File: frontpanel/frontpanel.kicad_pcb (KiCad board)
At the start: 2 copper layers, 50.5 x 128.5 mm, 13 parts

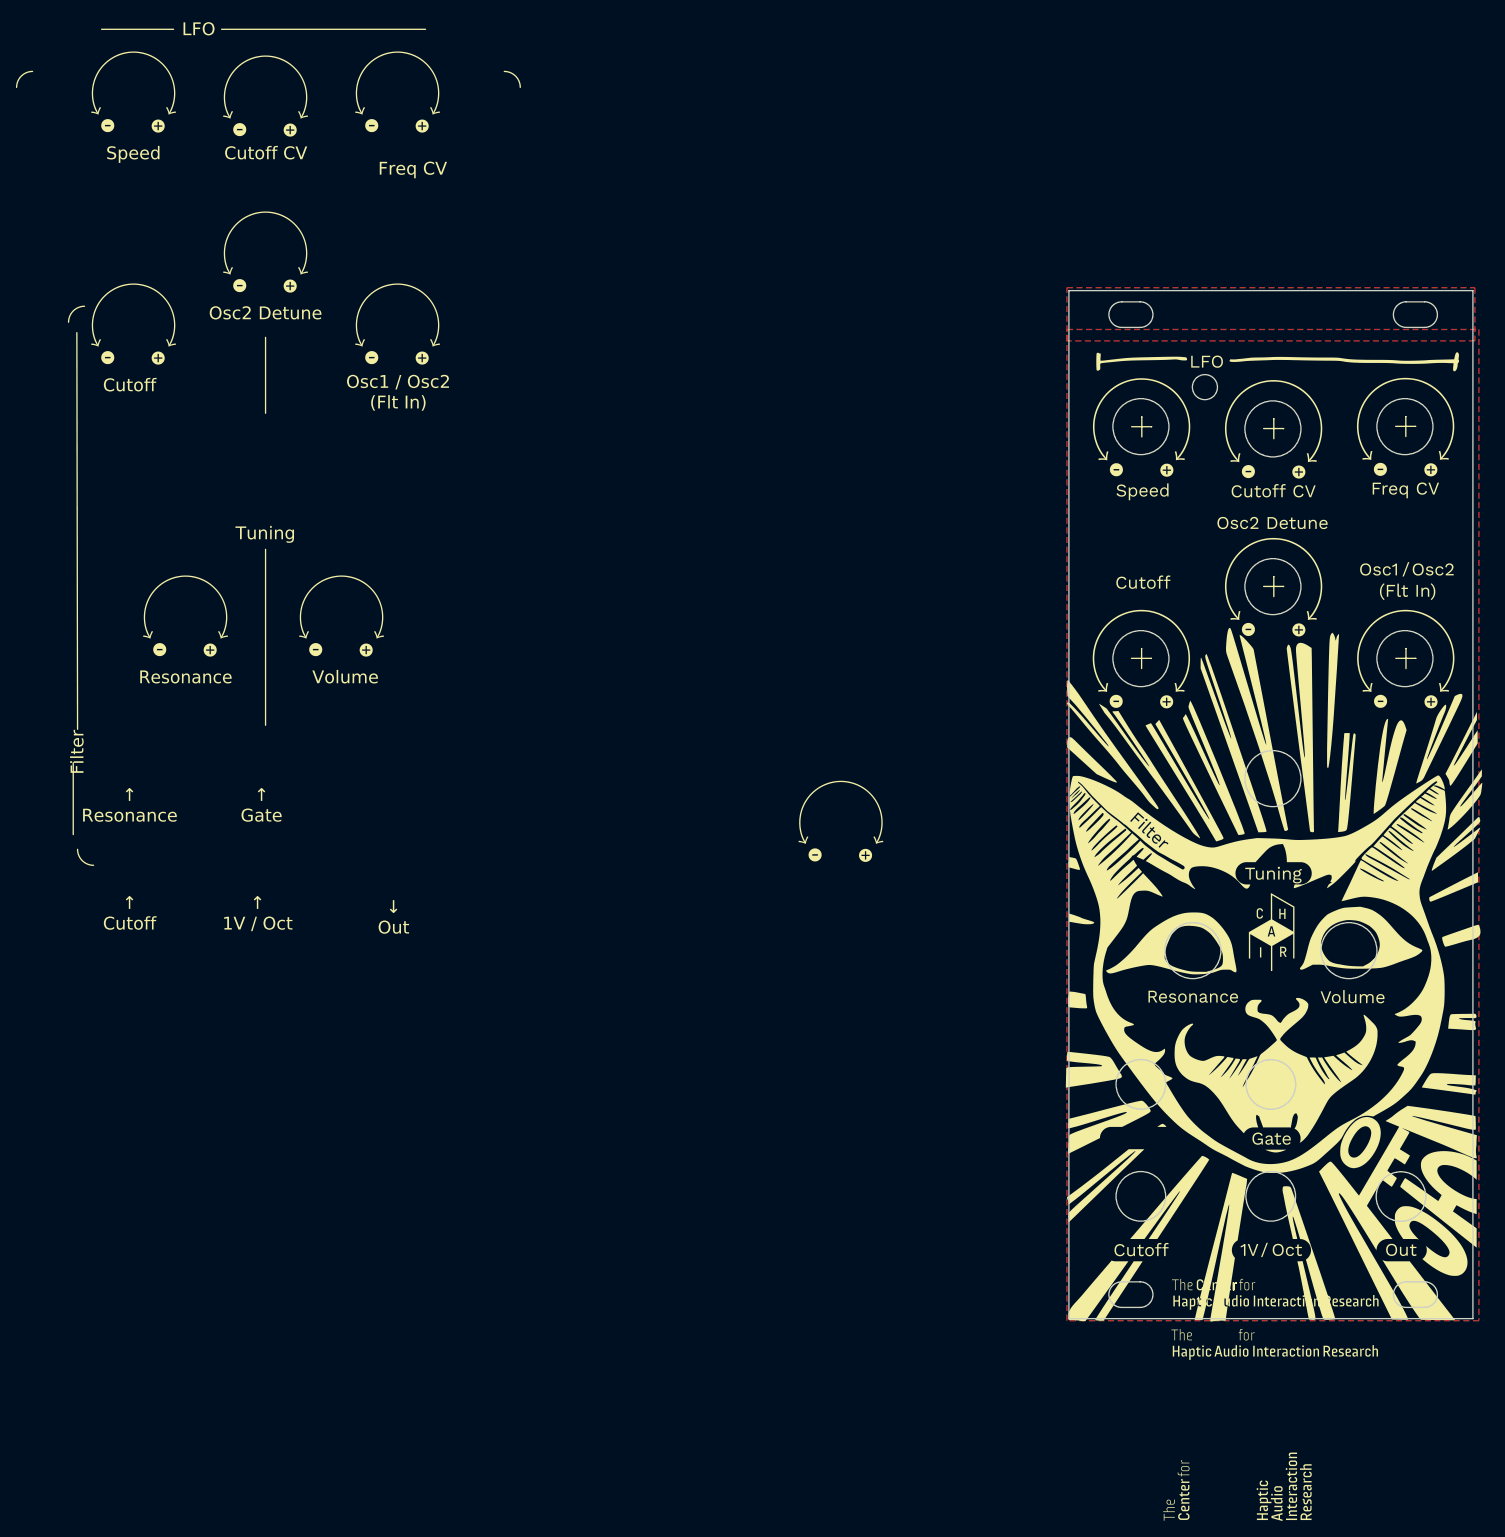
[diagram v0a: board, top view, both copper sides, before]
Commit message: Some fixes after evaluation of prototype
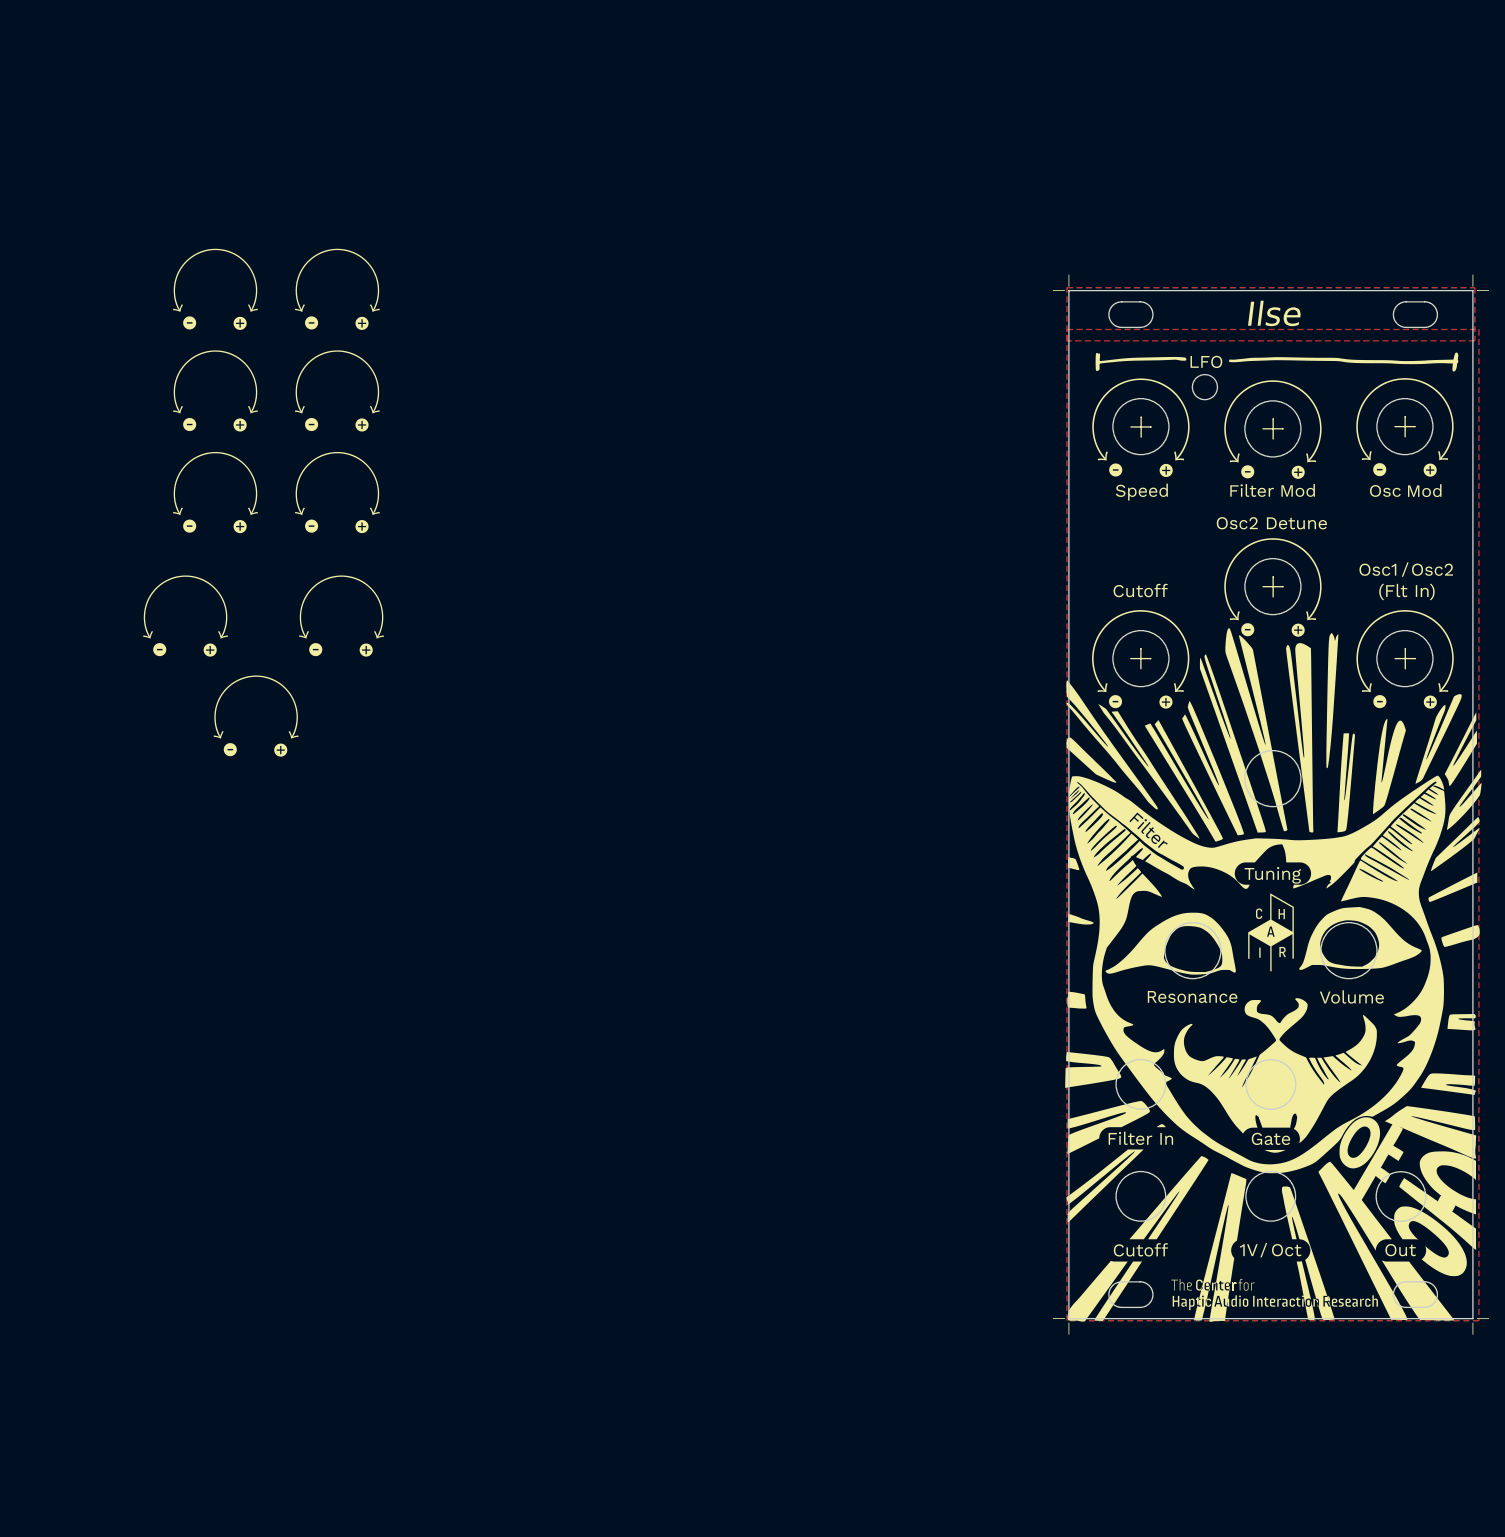
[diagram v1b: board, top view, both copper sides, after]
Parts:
- removed G***: LOGO, CHAIR:CHAIR_logo_horizontal_silkscreen+Cu
- moved REF** 74.3 mm to (-32.3, 90.2)
- moved REF** 51.1 mm to (-37.3, 62.2)
- moved REF** 33.1 mm to (-22.1, 62.2)
- moved REF** 25.8 mm to (-22.1, 36.8)
- moved REF** 25.0 mm to (-37.3, 36.8)
- moved REF** 18.5 mm to (-37.3, 49.5)
- moved REF** 11.2 mm to (-22.1, 49.5)
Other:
- board text removed: "Cutoff"
- board text removed: "Cutoff CV"
- board text removed: "Filter"
- board text removed: "Freq CV"
- board text removed: "LFO"
- board text removed: "Osc1 / Osc2 (Flt In)"
- board text removed: "Osc2 Detune"
- board text removed: "Resonance"
- board text removed: "Speed"
- board text removed: "Tuning"
- board text removed: "Volume"
- board text removed: "↑ 1V / Oct"
- board text removed: "↑ Cutoff"
- board text removed: "↑ Gate"
- board text removed: "↑ Resonance"
- board text removed: "↓ Out"

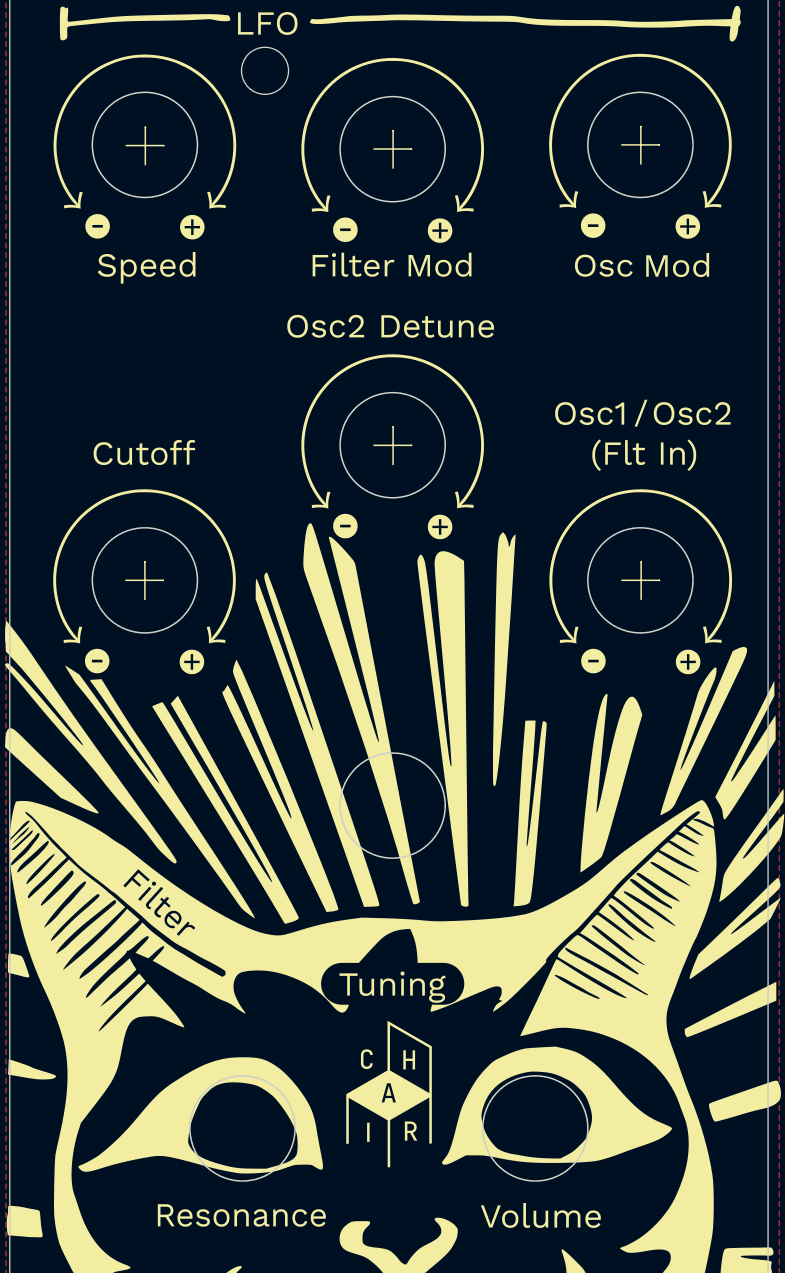
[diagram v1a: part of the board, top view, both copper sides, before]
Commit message: Some fixes after evaluation of prototype
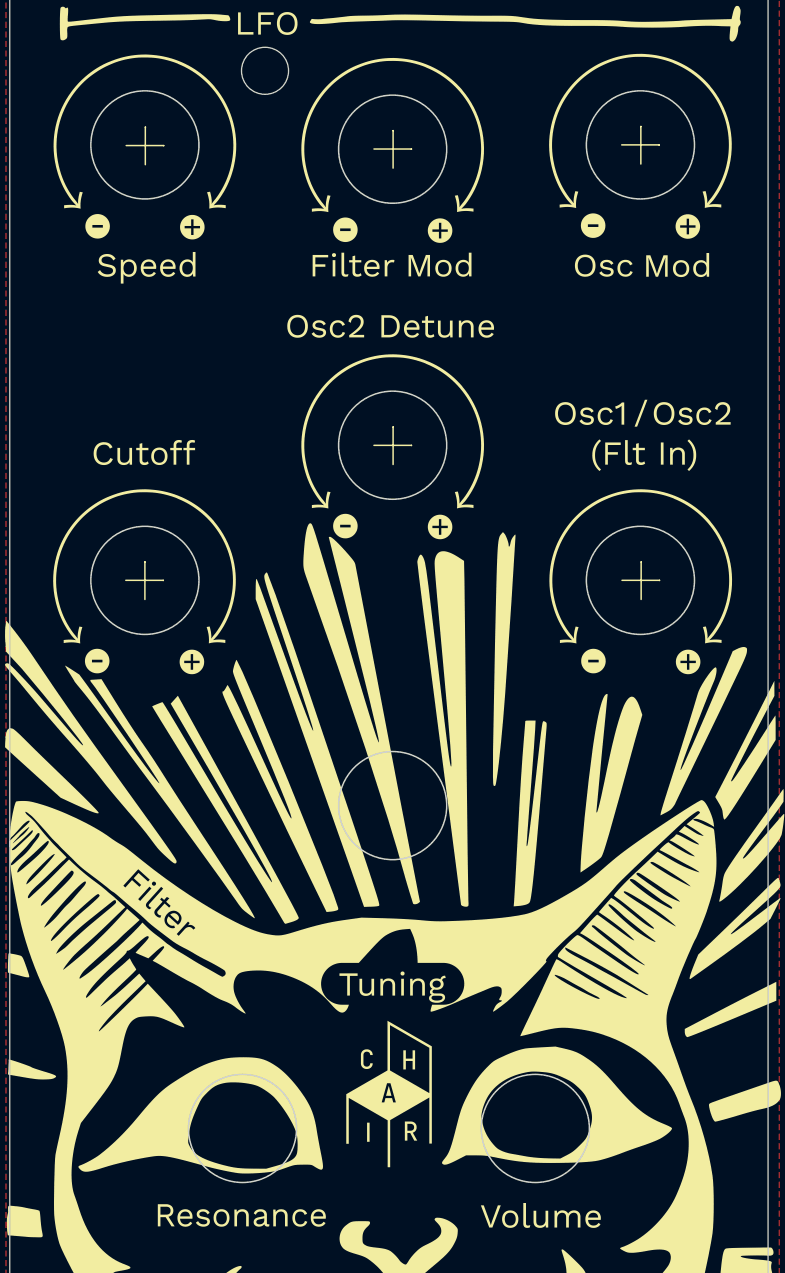
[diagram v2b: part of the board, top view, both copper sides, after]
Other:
- outline, holes or cut-outs redrawn
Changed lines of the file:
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@@
     )
     (stroke (width 0) (type solid)) (fill solid) (layer "F.SilkS"))
-  (gr_circle (center 104.342 119.33) (end 107.842 119.33)
+  (gr_circle (center 104.342 119.33) (end 107.942 119.33)
     (stroke (width 0.1) (type solid)) (fill none) (layer "Edge.Cuts"))
   (gr_circle (center 86.342 48.895972) (end 87.561681 49.878137)
@@
   (gr_circle (center 94.588724 136.057752) (end 97.688724 136.057752)
     (stroke (width 0.1) (type solid)) (fill none) (layer "Edge.Cuts"))
-  (gr_circle (center 111.342 53.83) (end 114.842 53.83)
+  (gr_circle (center 111.342 53.83) (end 114.942 53.83)
     (stroke (width 0.1) (type solid)) (fill none) (layer "Edge.Cuts"))
   (gr_line (start 69.342 165.33) (end 119.842 165.33)
@@
   (gr_line (start 119.842 36.83) (end 119.842 165.33)
     (stroke (width 0.05) (type solid)) (layer "Edge.Cuts"))
-  (gr_circle (center 111.342 82.83) (end 114.842 82.83)
+  (gr_circle (center 111.342 82.83) (end 114.942 82.83)
     (stroke (width 0.1) (type solid)) (fill none) (layer "Edge.Cuts"))
   (gr_line (start 119.842 36.83) (end 69.342 36.83)
@@
   (gr_circle (center 78.33491 150.045665) (end 81.43491 150.045665)
     (stroke (width 0.1) (type solid)) (fill none) (layer "Edge.Cuts"))
-  (gr_circle (center 94.842 54.115351) (end 98.342 54.115351)
+  (gr_circle (center 94.842 54.115351) (end 98.442 54.115351)
     (stroke (width 0.1) (type solid)) (fill none) (layer "Edge.Cuts"))
-  (gr_circle (center 78.342 82.83) (end 81.842 82.83)
+  (gr_circle (center 78.342 82.83) (end 81.942 82.83)
     (stroke (width 0.1) (type solid)) (fill none) (layer "Edge.Cuts"))
-  (gr_circle (center 84.842 119.33) (end 88.342 119.33)
+  (gr_circle (center 84.842 119.33) (end 88.442 119.33)
     (stroke (width 0.1) (type solid)) (fill none) (layer "Edge.Cuts"))
-  (gr_circle (center 94.842 73.83) (end 98.342 73.83)
+  (gr_circle (center 94.842 73.83) (end 98.442 73.83)
     (stroke (width 0.1) (type solid)) (fill none) (layer "Edge.Cuts"))
-  (gr_circle (center 94.842 97.83) (end 98.342 97.83)
+  (gr_circle (center 94.842 97.83) (end 98.442 97.83)
     (stroke (width 0.1) (type solid)) (fill none) (layer "Edge.Cuts"))
-  (gr_circle (center 78.342 53.83) (end 81.842 53.83)
+  (gr_circle (center 78.342 53.83) (end 81.942 53.83)
     (stroke (width 0.1) (type solid)) (fill none) (layer "Edge.Cuts"))
   (gr_line (start 69.342 165.33) (end 69.342 36.83)

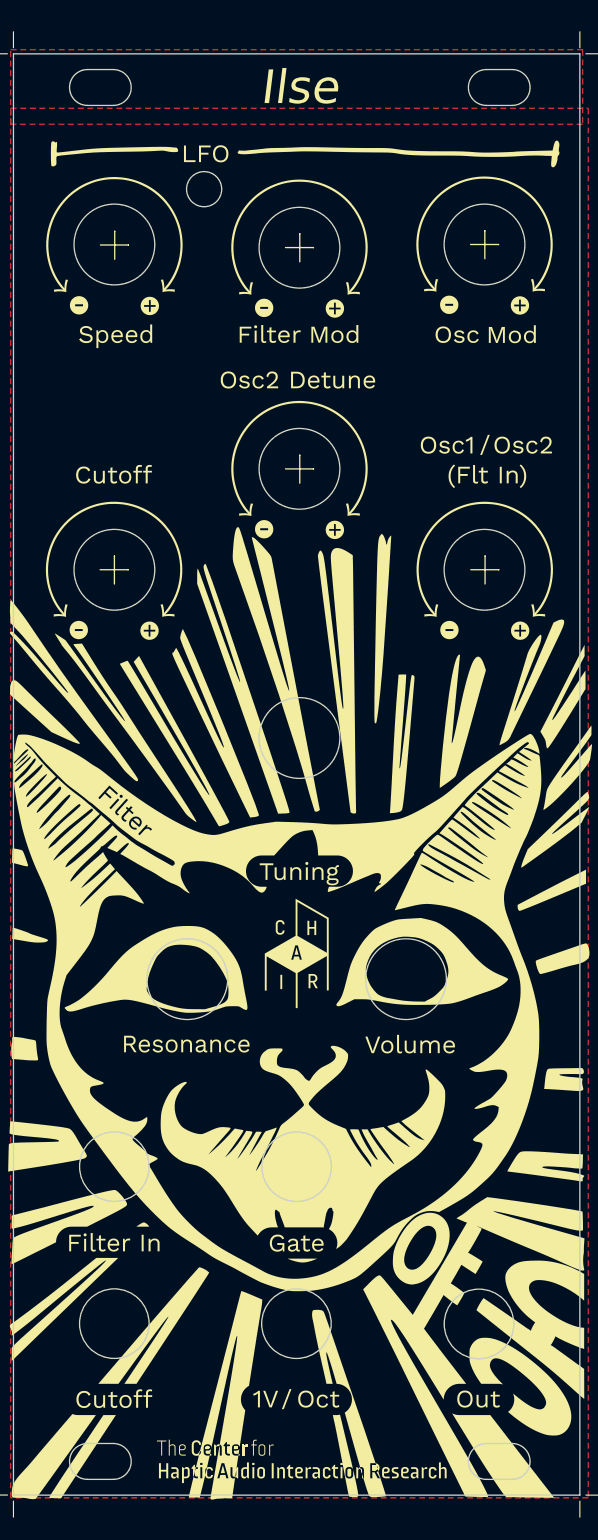
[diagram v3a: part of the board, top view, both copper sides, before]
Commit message: turned transistors around
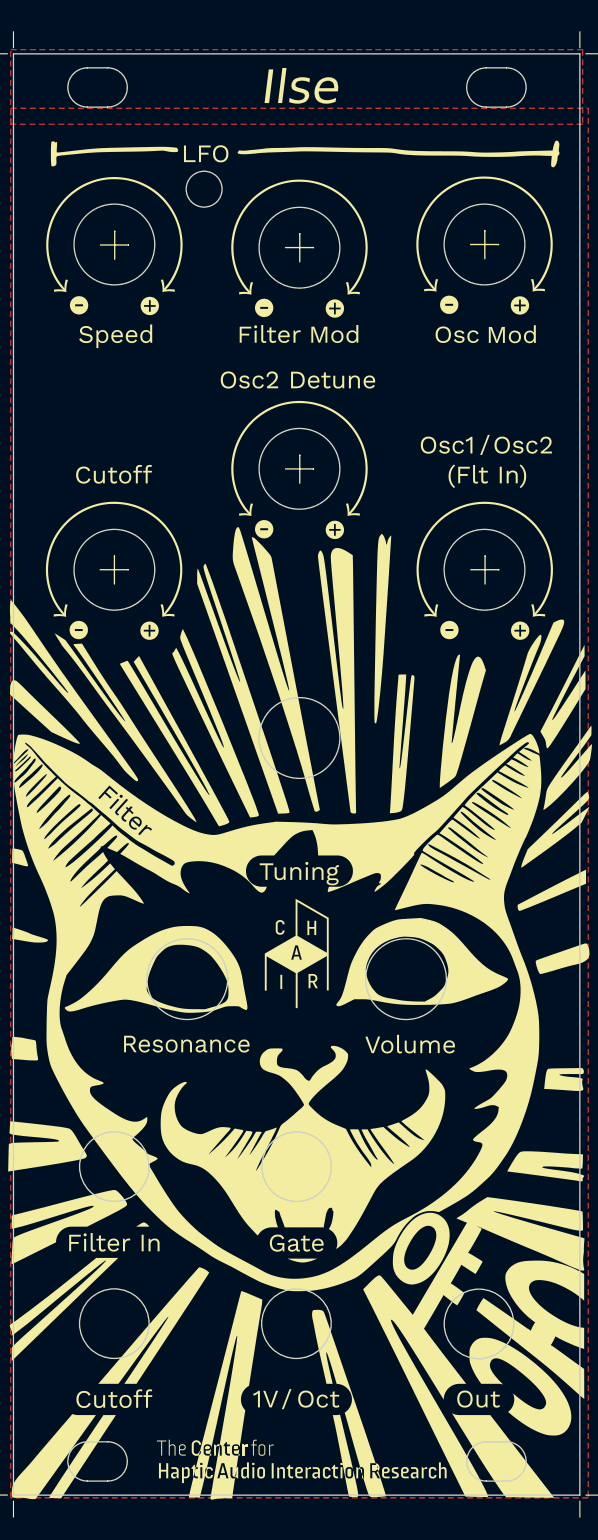
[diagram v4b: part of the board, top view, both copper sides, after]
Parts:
- H1, H2: footprint CHAIR:MountingHole_Eurorack_3U_slotted -> CHAIR:MountingHole_Eurorack_3U_slotted_grawart
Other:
- outline, holes or cut-outs redrawn

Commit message: REV4 documentation and iBOM added
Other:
- board text added: "10 HP"
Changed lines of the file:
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@@
     )
+  )
+  (gr_text "10 HP" (at 92.202 179.07) (layer "Cmts.User")
+    (effects (font (size 1 1) (thickness 0.15)) (justify left bottom))
   )
   (dimension (type orthogonal) (layer "Dwgs.User")
